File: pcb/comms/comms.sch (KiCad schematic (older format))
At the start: 48 parts, among them IC1 STM32F437VIT6, IC2 ADP3335, IC3 MAX14787E, IC4 RJHSE-538x, J1 UART1, J2 UART2, J3 5v In, P1 USB-B, P2 SWD_TC, X1 USB Conn, X2 USB Cap, X3 RJ45 Conn, X4 RJ45 Cap, X5 Hole, X6 Hole, X7 Case, X8 Hole, X9 Hole, Y1 26M

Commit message: finished comms board
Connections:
- net 5v: no longer C18.1
- net LED1: now also IC1.2 (PE3); no longer IC1.45 (PE14)
- net LED2: now also IC1.1 (PE2); no longer IC1.46 (PE15)
- net OTG_HS_VBUS: now also C18.1
- net STATUS: now also IC1.51 (PB12); no longer IC1.64 (PC7)
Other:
- note added: "NF J3 on PC Side"
- note removed: "NF J3/C18 on PC Side"
- moved on the sheet: C18, J3
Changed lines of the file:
@@
 encoding utf-8
 Sheet 1 1
-Title ""
-Date "2018-11-09"
-Rev ""
-Comp ""
-Comment1 ""
+Title "Communications Board"
+Date "2018-11-11"
+Rev "1"
+Comp "Matthew Coates"
+Comment1 "Hybrid Ignition Controller"
 Comment2 ""
 Comment3 ""
@@
 Wire Wire Line
 	1175 1725 1175 1625
-Text Label 3125 1925 0    50   ~ 0
+Text Label 1725 6825 2    50   ~ 0
 STATUS
 $Comp
@@
 	1825 4025 1725 4025
 Wire Wire Line
-	3025 1925 3125 1925
+	1825 6825 1725 6825
 NoConn ~ 3025 6225
 NoConn ~ 3025 6025
@@
 NoConn ~ 3025 5325
 NoConn ~ 3025 5225
-NoConn ~ 3025 5125
 NoConn ~ 3025 4925
 NoConn ~ 3025 4825
@@
 U 1 1 5C1B4CC6
 P 9900 2900
-F 0 "P2" H 9900 3225 50  0000 C CNN
-F 1 "SWD_TC" H 9900 3134 50  0000 C CNN
+F 0 "P2" H 9650 3100 50  0000 C CNN
+F 1 "SWD_TC" H 9725 2700 50  0000 C CNN
 F 2 "agg:TC2030-NL" H 9600 2600 50  0001 L CNN
 F 3 "" H 9506 3000 50  0001 C CNN
@@
 U 1 1 5C1B4CCE
 P 9300 3050
-F 0 "C19" V 9375 3125 39  0000 C CNN
+F 0 "C19" V 9375 3150 39  0000 C CNN
 F 1 "100n" V 9300 3150 39  0000 C CNN
 F 2 "agg:0402" H 9300 3050 50  0001 C CNN
@@
 L agg-kicad:CONN_01x02 J3
 U 1 1 5C1B4D20
-P 8200 1150
-F 0 "J3" H 8175 1250 50  0000 C CNN
-F 1 "5v In" H 8200 950 50  0000 C CNN
-F 2 "agg:S02B-PASK-2" H 8200 1150 50  0001 C CNN
-F 3 "" H 8200 1150 50  0001 C CNN
-F 4 "1830747" H 8200 1150 50  0001 C CNN "Farnell"
-	1    8200 1150
+P 8250 1225
+F 0 "J3" H 8225 1325 50  0000 C CNN
+F 1 "5v In" H 8250 1025 50  0000 C CNN
+F 2 "agg:S02B-PASK-2" H 8250 1225 50  0001 C CNN
+F 3 "" H 8250 1225 50  0001 C CNN
+F 4 "1830747" H 8250 1225 50  0001 C CNN "Farnell"
+	1    8250 1225
 	1    0    0    -1
 $EndComp
@@
 L agg-kicad:GND #PWR021
 U 1 1 5C1B4D27
-P 8400 1350
-F 0 "#PWR021" H 8270 1390 50  0001 L CNN
-F 1 "GND" H 8400 1250 50  0000 C CNN
-F 2 "" H 8400 1350 50  0001 C CNN
-F 3 "" H 8400 1350 50  0001 C CNN
-	1    8400 1350
-	1    0    0    -1
-$EndComp
-Wire Wire Line
-	8300 1250 8400 1250
+P 8450 1425
+F 0 "#PWR021" H 8320 1465 50  0001 L CNN
+F 1 "GND" H 8450 1325 50  0000 C CNN
+F 2 "" H 8450 1425 50  0001 C CNN
+F 3 "" H 8450 1425 50  0001 C CNN
+	1    8450 1425
+	1    0    0    -1
+$EndComp
+Wire Wire Line
+	8350 1325 8450 1325
 $Comp
 L agg-kicad:5v #PWR022
 U 1 1 5C1B4D2E
-P 8600 1050
-F 0 "#PWR022" H 8600 1160 50  0001 L CNN
-F 1 "5v" H 8600 1174 50  0000 C CNN
-F 2 "" H 8600 1050 50  0001 C CNN
-F 3 "" H 8600 1050 50  0001 C CNN
-	1    8600 1050
-	1    0    0    -1
-$EndComp
-$Comp
-L agg-kicad:5v #PWR023
-U 1 1 5C1B4D36
-P 8800 1050
-F 0 "#PWR023" H 8800 1160 50  0001 L CNN
-F 1 "5v" H 8800 1174 50  0000 C CNN
-F 2 "" H 8800 1050 50  0001 C CNN
-F 3 "" H 8800 1050 50  0001 C CNN
-	1    8800 1050
+P 8650 1125
+F 0 "#PWR022" H 8650 1235 50  0001 L CNN
+F 1 "5v" H 8650 1249 50  0000 C CNN
+F 2 "" H 8650 1125 50  0001 C CNN
+F 3 "" H 8650 1125 50  0001 C CNN
+	1    8650 1125
 	1    0    0    -1
 $EndComp
@@
 L agg-kicad:GND #PWR024
 U 1 1 5C1B4D3C
-P 8800 1350
-F 0 "#PWR024" H 8670 1390 50  0001 L CNN
-F 1 "GND" H 8800 1250 50  0000 C CNN
-F 2 "" H 8800 1350 50  0001 C CNN
-F 3 "" H 8800 1350 50  0001 C CNN
-	1    8800 1350
-	1    0    0    -1
-$EndComp
-Wire Wire Line
-	8800 1250 8800 1350
-Wire Wire Line
-	8800 1150 8800 1050
+P 5875 2525
+F 0 "#PWR024" H 5745 2565 50  0001 L CNN
+F 1 "GND" H 5875 2425 50  0000 C CNN
+F 2 "" H 5875 2525 50  0001 C CNN
+F 3 "" H 5875 2525 50  0001 C CNN
+	1    5875 2525
+	1    0    0    -1
+$EndComp
 Text Notes 4400 2350 0    79   ~ 16
 USB Input:
@@
 L agg-kicad:5v #PWR012
 U 1 1 5C252DEC
-P 5450 2475
-F 0 "#PWR012" H 5450 2585 50  0001 L CNN
-F 1 "5v" H 5450 2599 50  0000 C CNN
-F 2 "" H 5450 2475 50  0001 C CNN
-F 3 "" H 5450 2475 50  0001 C CNN
-	1    5450 2475
+P 5450 2525
+F 0 "#PWR012" H 5450 2635 50  0001 L CNN
+F 1 "5v" H 5450 2649 50  0000 C CNN
+F 2 "" H 5450 2525 50  0001 C CNN
+F 3 "" H 5450 2525 50  0001 C CNN
+	1    5450 2525
 	1    0    0    -1
 $EndComp
@@
 	5350 2575 5450 2575
 Wire Wire Line
-	5450 2575 5450 2475
-Wire Wire Line
-	8600 1150 8600 1050
+	8650 1225 8650 1125
 $Comp
 L agg-kicad:C C18
 U 1 1 5C2EC01C
-P 8800 1150
-F 0 "C18" V 8812 1208 39  0000 L CNN
-F 1 "1u" V 8887 1208 39  0000 L CNN
-F 2 "agg:0603-L" H 8800 1150 50  0001 C CNN
-F 3 "" H 8800 1150 50  0001 C CNN
-F 4 "1865556" H 8800 1150 60  0001 C CNN "Farnell"
-	1    8800 1150
+P 5875 2375
+F 0 "C18" V 5887 2433 39  0000 L CNN
+F 1 "1u" V 5962 2433 39  0000 L CNN
+F 2 "agg:0603-L" H 5875 2375 50  0001 C CNN
+F 3 "" H 5875 2375 50  0001 C CNN
+F 4 "1865556" H 5875 2375 60  0001 C CNN "Farnell"
+	1    5875 2375
 	0    1    1    0
 $EndComp
-Text Notes 8025 700  0    79   ~ 16
+Text Notes 7900 725  0    79   ~ 16
 External Supply:
-Text Notes 4350 3750 0    79   ~ 16
+Text Notes 4400 3775 0    79   ~ 16
 RS485 Driver:
 Wire Notes Line
@@
 NoConn ~ 3025 2525
 NoConn ~ 3025 3225
-NoConn ~ 3025 5025
 NoConn ~ 3025 5525
 NoConn ~ 3025 5725
@@
 NoConn ~ 1825 6425
 NoConn ~ 1825 6525
-NoConn ~ 1825 6825
 NoConn ~ 1825 5625
 NoConn ~ 1825 5725
@@
 Wire Wire Line
 	7400 4175 7550 4175
-Text Label 3125 6325 0    50   ~ 0
+Text Label 3125 5125 0    50   ~ 0
 LED1
-Text Label 3125 6425 0    50   ~ 0
+Text Label 3125 5025 0    50   ~ 0
 LED2
 Wire Wire Line
@@
 	7500 4375 7500 4675
 Wire Wire Line
-	3025 6325 3125 6325
-Wire Wire Line
-	3125 6425 3025 6425
+	3025 5025 3125 5025
+Wire Wire Line
+	3125 5125 3025 5125
 $Comp
 L agg-kicad:PART X7
@@
 Crossover Cable Required!
 Wire Wire Line
-	8400 1350 8400 1250
+	8450 1425 8450 1325
 Text Notes 7625 3475 0    50   Italic 0
 NF J1/J2 on PC Side
-Text Notes 8125 1700 0    50   Italic 0
-NF J3/C18 on PC Side
-Wire Wire Line
-	8300 1150 8600 1150
+Text Notes 7875 2025 0    50   Italic 0
+NF J3 on PC Side
+Wire Wire Line
+	8350 1225 8650 1225
 Text Notes 5425 3475 0    50   Italic 0
 NF R2 on \nController Side
+Wire Wire Line
+	5875 2475 5875 2525
+Text Label 5850 2275 2    50   ~ 0
+OTG_HS_VBUS
+Wire Wire Line
+	5850 2275 5875 2275
+Wire Wire Line
+	5875 2275 5875 2375
+Wire Wire Line
+	5450 2525 5450 2575
+NoConn ~ 3025 6425
+NoConn ~ 3025 6325
+NoConn ~ 3025 1925
 $EndSCHEMATC

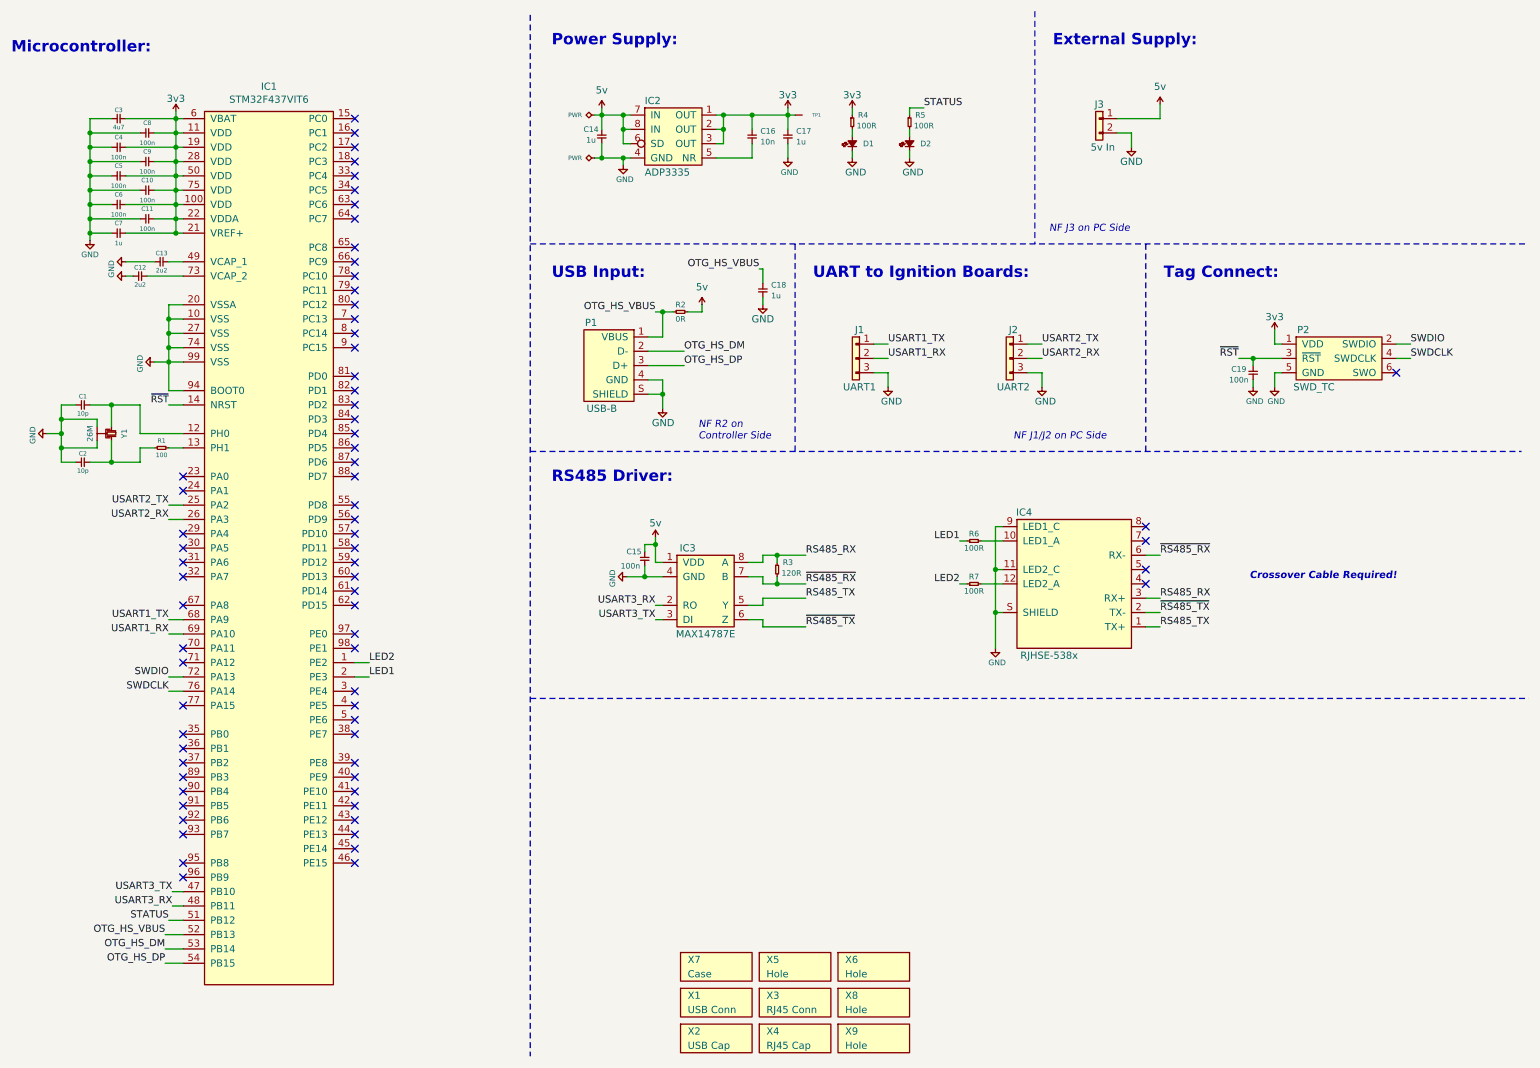
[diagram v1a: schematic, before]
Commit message: made changes to comms as per review
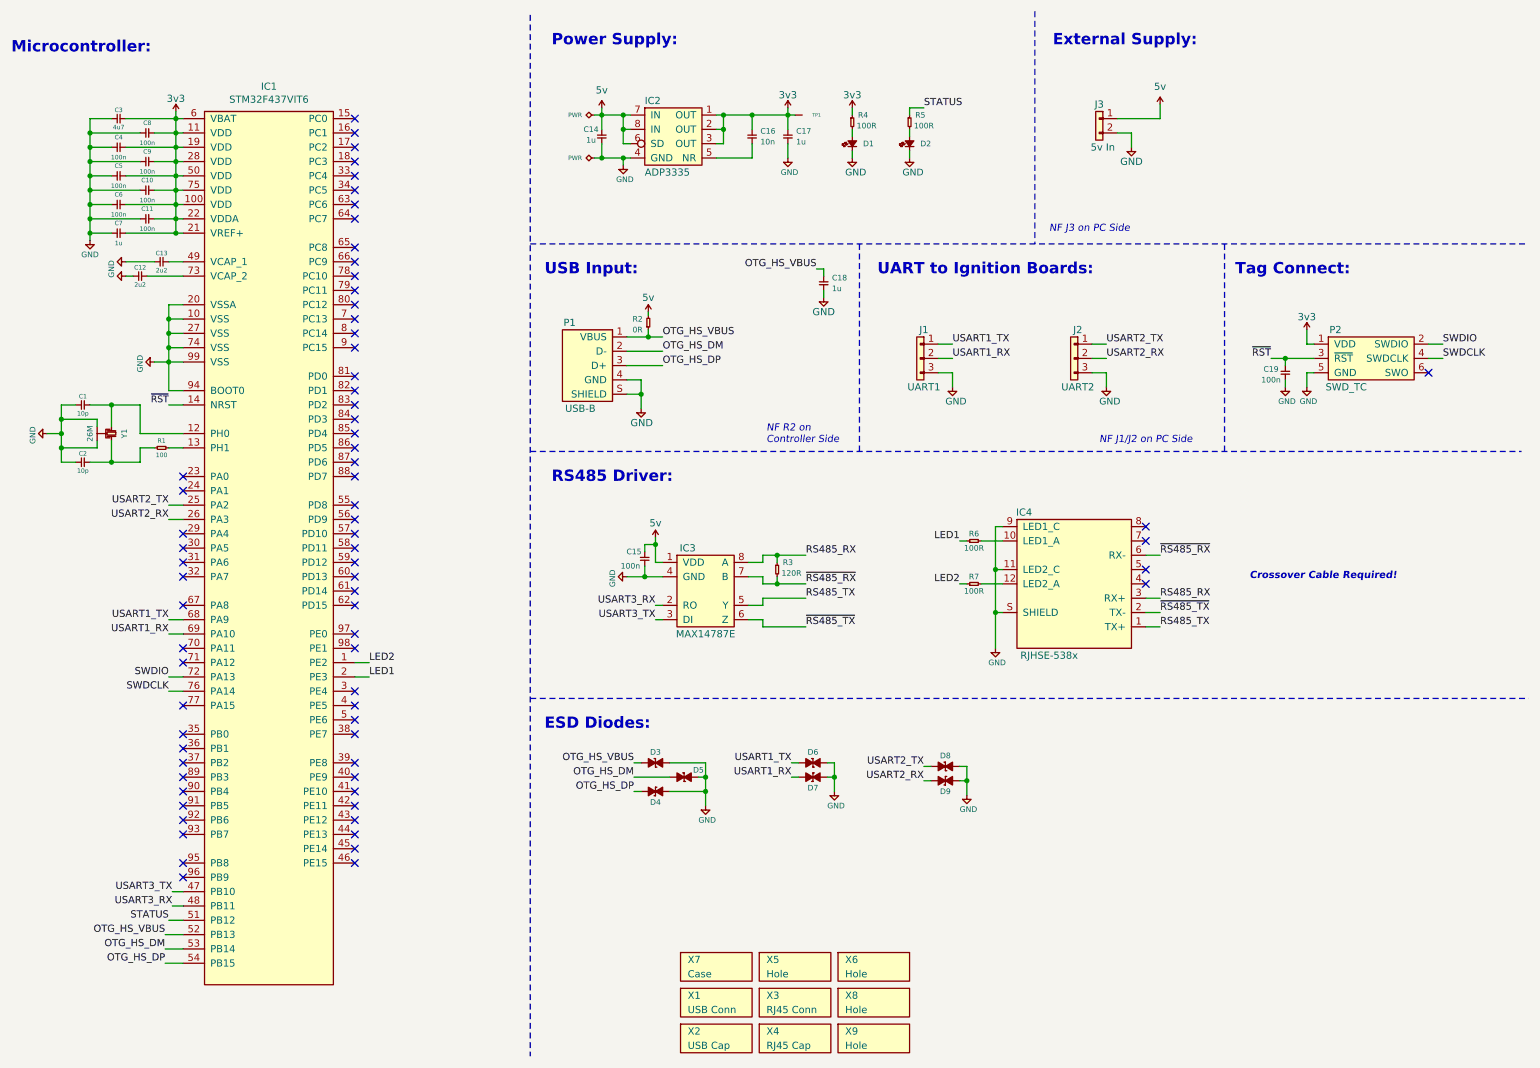
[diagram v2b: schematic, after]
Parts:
- added D3, D4, D5, D6, D7, D8, D9: ESD_DIODE, agg:0402, symbol agg-kicad:ESD_DIODE
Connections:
- net GND: now also D3.2, D4.2, D5.2, D6.2, D7.2, D8.2, D9.2
- net OTG_HS_DM: now also D5.1
- net OTG_HS_DP: now also D4.1
- net OTG_HS_VBUS: now also D3.1
- net USART1_RX: now also D7.1
- net USART1_TX: now also D6.1
- net USART2_RX: now also D9.1
- net USART2_TX: now also D8.1
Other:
- note added: "ESD Diodes:"
- moved on the sheet: C18, C19, J1, J2, P1, P2, R2
